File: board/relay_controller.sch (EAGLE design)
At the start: 77 parts, among them IC1 STM32F103C8T, IC3 AT24C, K1 G6K-2F-Y, K2 G6K-2F-Y, K3 G6K-2F-Y, K7 G6K-2F-Y, K8 G6K-2F-Y, Q1 220mA/50V/3.5Ω, Q2 220mA/50V/3.5Ω, Q3 220mA/50V/3.5Ω, Q4 220mA/50V/3.5Ω, Q5 220mA/50V/3.5Ω, X1 RJ45-8L21-S, X2 RJ45-8L21-S

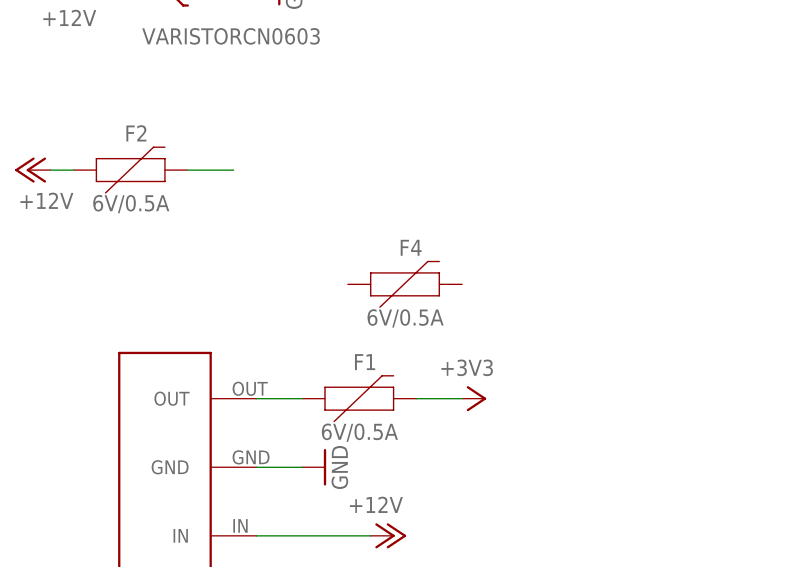
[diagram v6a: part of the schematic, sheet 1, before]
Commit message: remove unused fuse
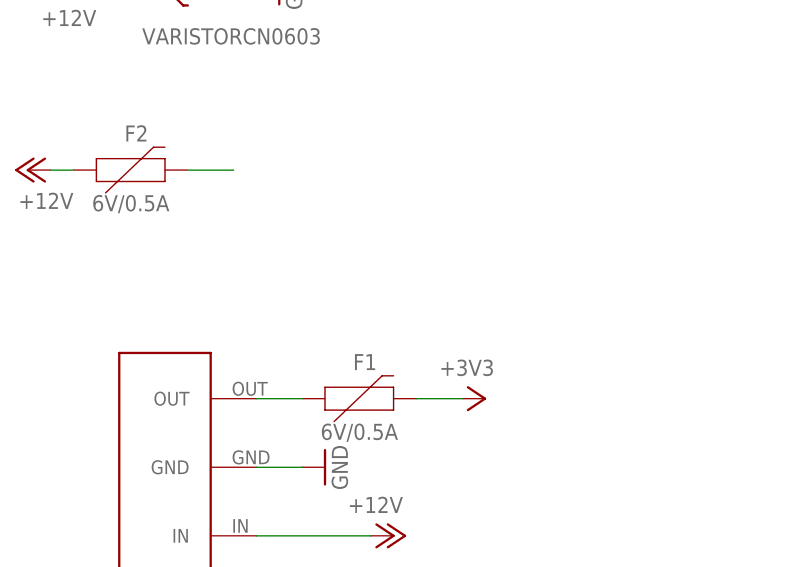
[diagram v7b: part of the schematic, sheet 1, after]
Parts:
- removed F4: 6V/0.5A, SparkFun-Fuses:PPTC_HALF-AMP
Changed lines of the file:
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@@
 <part name="C10" library="microbuilder" deviceset="CAP_CERAMIC" device="0603" value="33pf"/>
 <part name="C2" library="microbuilder" deviceset="CAP_CERAMIC" device="0603" value="10nF"/>
-<part name="F4" library="SparkFun-Fuses" deviceset="PPTC" device="_HALF-AMP" value="6V/0.5A"/>
 </parts>
 <sheets>
@@
 <instance part="C10" gate="G$1" x="-55.88" y="60.96" rot="R90"/>
 <instance part="C2" gate="G$1" x="-198.12" y="71.12"/>
-<instance part="F4" gate="G$1" x="114.3" y="12.7"/>
 </instances>
 <busses>

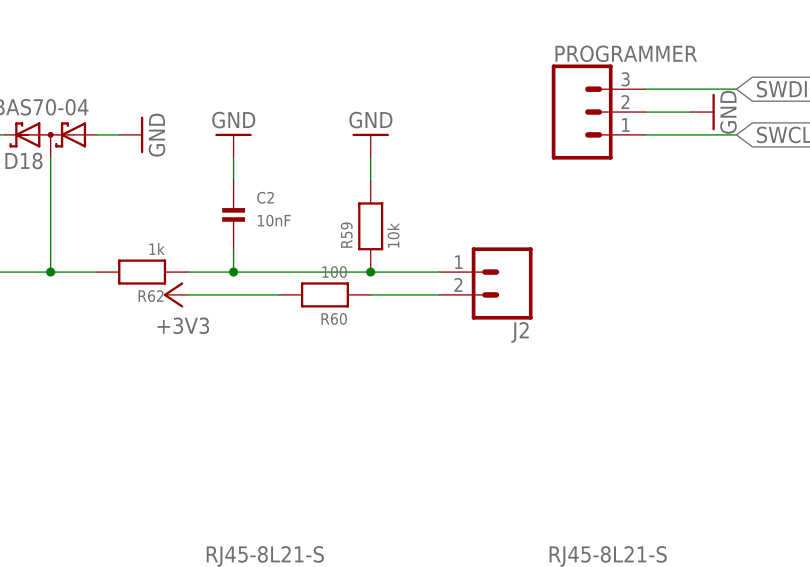
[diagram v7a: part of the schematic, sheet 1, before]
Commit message: fix labels and place orientation
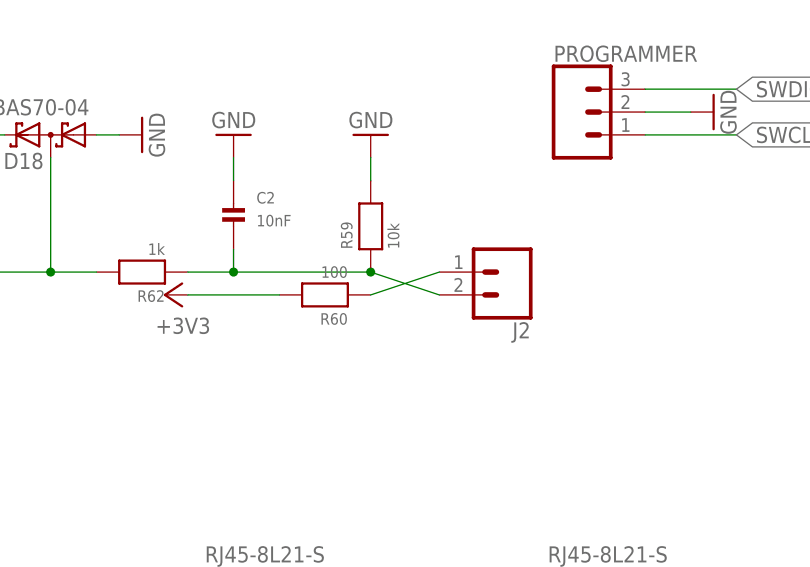
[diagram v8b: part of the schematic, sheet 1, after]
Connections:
- net N$10: now also J2.1; no longer J2.2
- net N$5: now also J2.2; no longer J2.1
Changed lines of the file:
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@@
 <segment>
 <pinref part="R60" gate="G$1" pin="1"/>
-<wire x1="-182.88" y1="63.5" x2="-175.26" y2="63.5" width="0.1524" layer="91"/>
-<pinref part="J2" gate="G$1" pin="2"/>
+<wire x1="-182.88" y1="63.5" x2="-175.26" y2="66.04" width="0.1524" layer="91"/>
+<pinref part="J2" gate="G$1" pin="1"/>
 </segment>
 </net>
@@
 <wire x1="-182.88" y1="66.04" x2="-198.12" y2="66.04" width="0.1524" layer="91"/>
 <junction x="-182.88" y="66.04"/>
-<wire x1="-175.26" y1="66.04" x2="-182.88" y2="66.04" width="0.1524" layer="91"/>
+<wire x1="-175.26" y1="63.5" x2="-182.88" y2="66.04" width="0.1524" layer="91"/>
 <pinref part="R62" gate="G$1" pin="1"/>
 <wire x1="-203.2" y1="66.04" x2="-198.12" y2="66.04" width="0.1524" layer="91"/>
 <junction x="-198.12" y="66.04"/>
-<pinref part="J2" gate="G$1" pin="1"/>
+<pinref part="J2" gate="G$1" pin="2"/>
 <pinref part="C2" gate="G$1" pin="P$2"/>
 </segment>
